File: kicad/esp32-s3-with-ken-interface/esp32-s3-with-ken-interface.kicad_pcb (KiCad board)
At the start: 4 copper layers, 50.8 x 81.3 mm, 40 parts, among them J1 TYPE-C-31-M-12, Q1 UMH3N, SW1 TSC015A03526A, SW2 TSC015A03526A, SW3 TSC015A03526A, U1 CH340C, U2 AMS1117-3.3, U3 XDZ254-2-15-W-2.5-G1, U4 ESP32-S3-WROOM-1, U5 PM254-2-15-W-8.5

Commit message: update symbol
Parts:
- moved U2 0.15 mm to (83.8, 83.5)

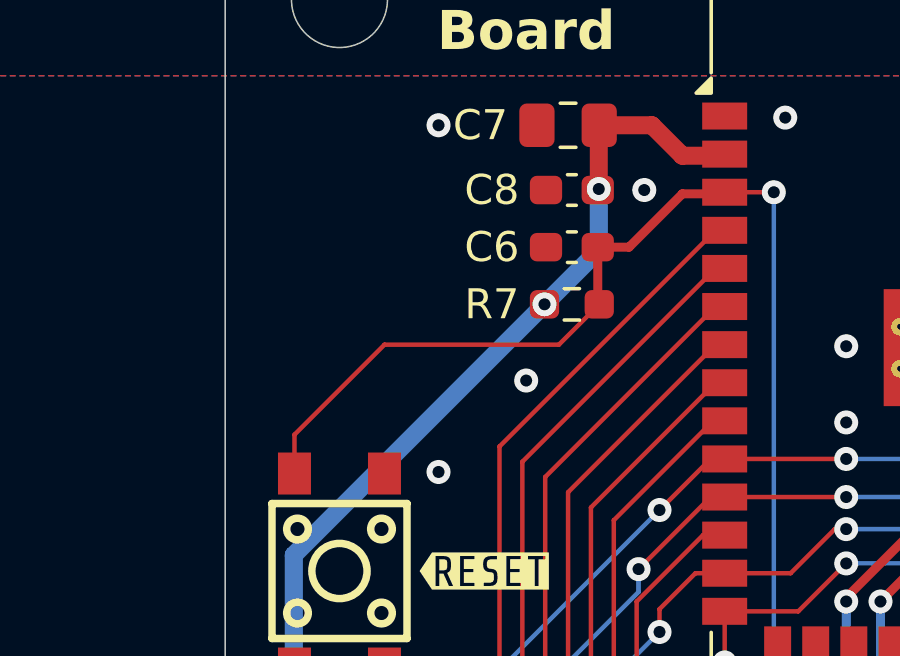
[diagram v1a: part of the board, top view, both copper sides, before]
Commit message: add capacitor
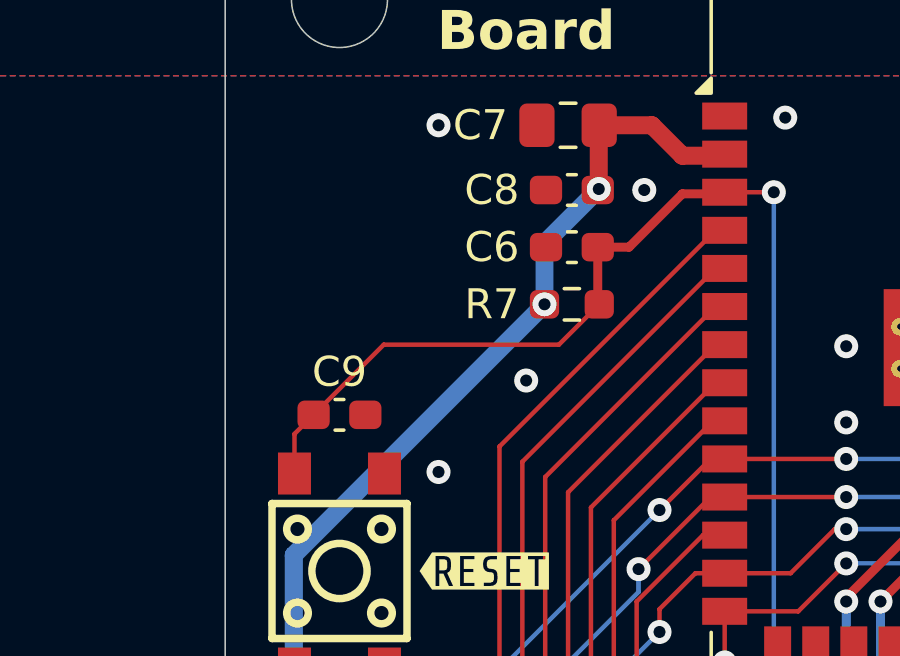
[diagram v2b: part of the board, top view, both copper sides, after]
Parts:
- added C9: 100nF, Capacitor_SMD:C_0603_1608Metric_Pad1.08x0.95mm_HandSolder, F.Cu at (62.2, 57.0)
